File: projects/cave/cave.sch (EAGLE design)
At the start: 111 parts, among them U1 IRLML6344TRPBF, U10 IRLML6344TRPBF, U11 IRLML6344TRPBF, U12 IRLML6344TRPBF, U2 TLC555CDR, U3 IRLML6344TRPBF, U4 IRLML6344TRPBF, U5 IRLML6344TRPBF, U6 IRLML6344TRPBF, U7 TPS54625, U9 IRLML6344TRPBF

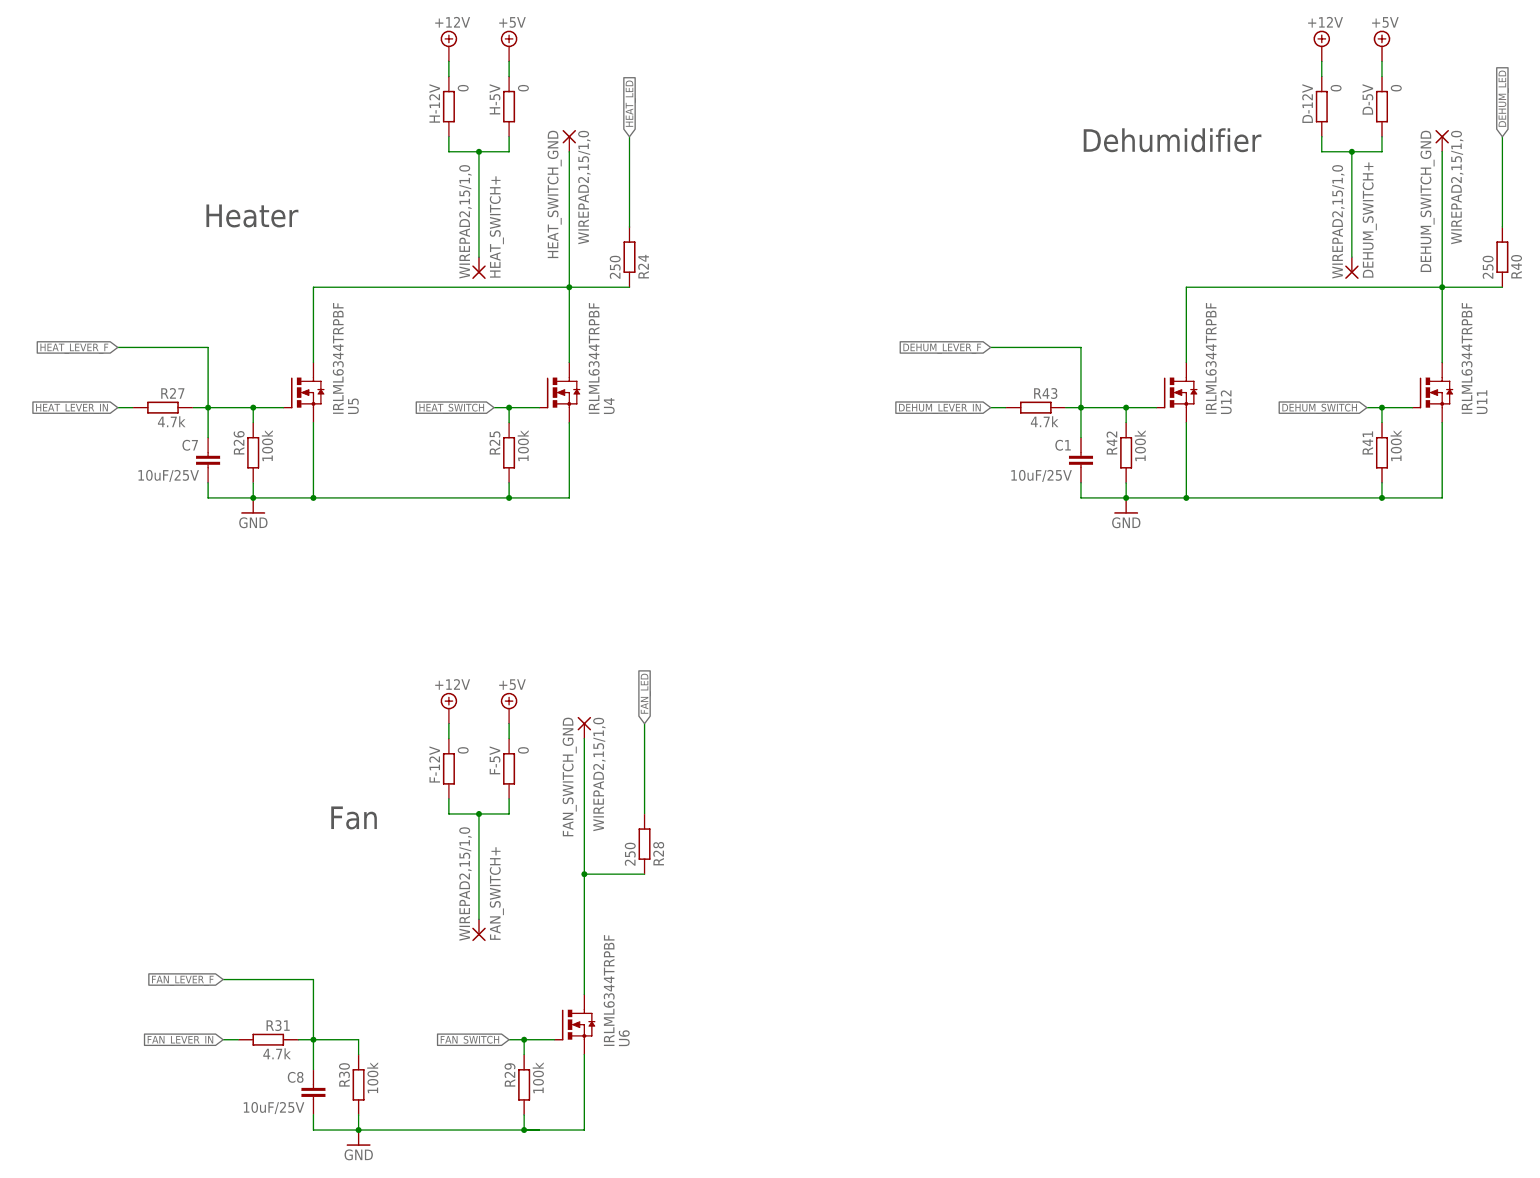
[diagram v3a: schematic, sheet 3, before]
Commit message: Changed 250ohm-0603 led res to 255ohm-0805. Generated BOM
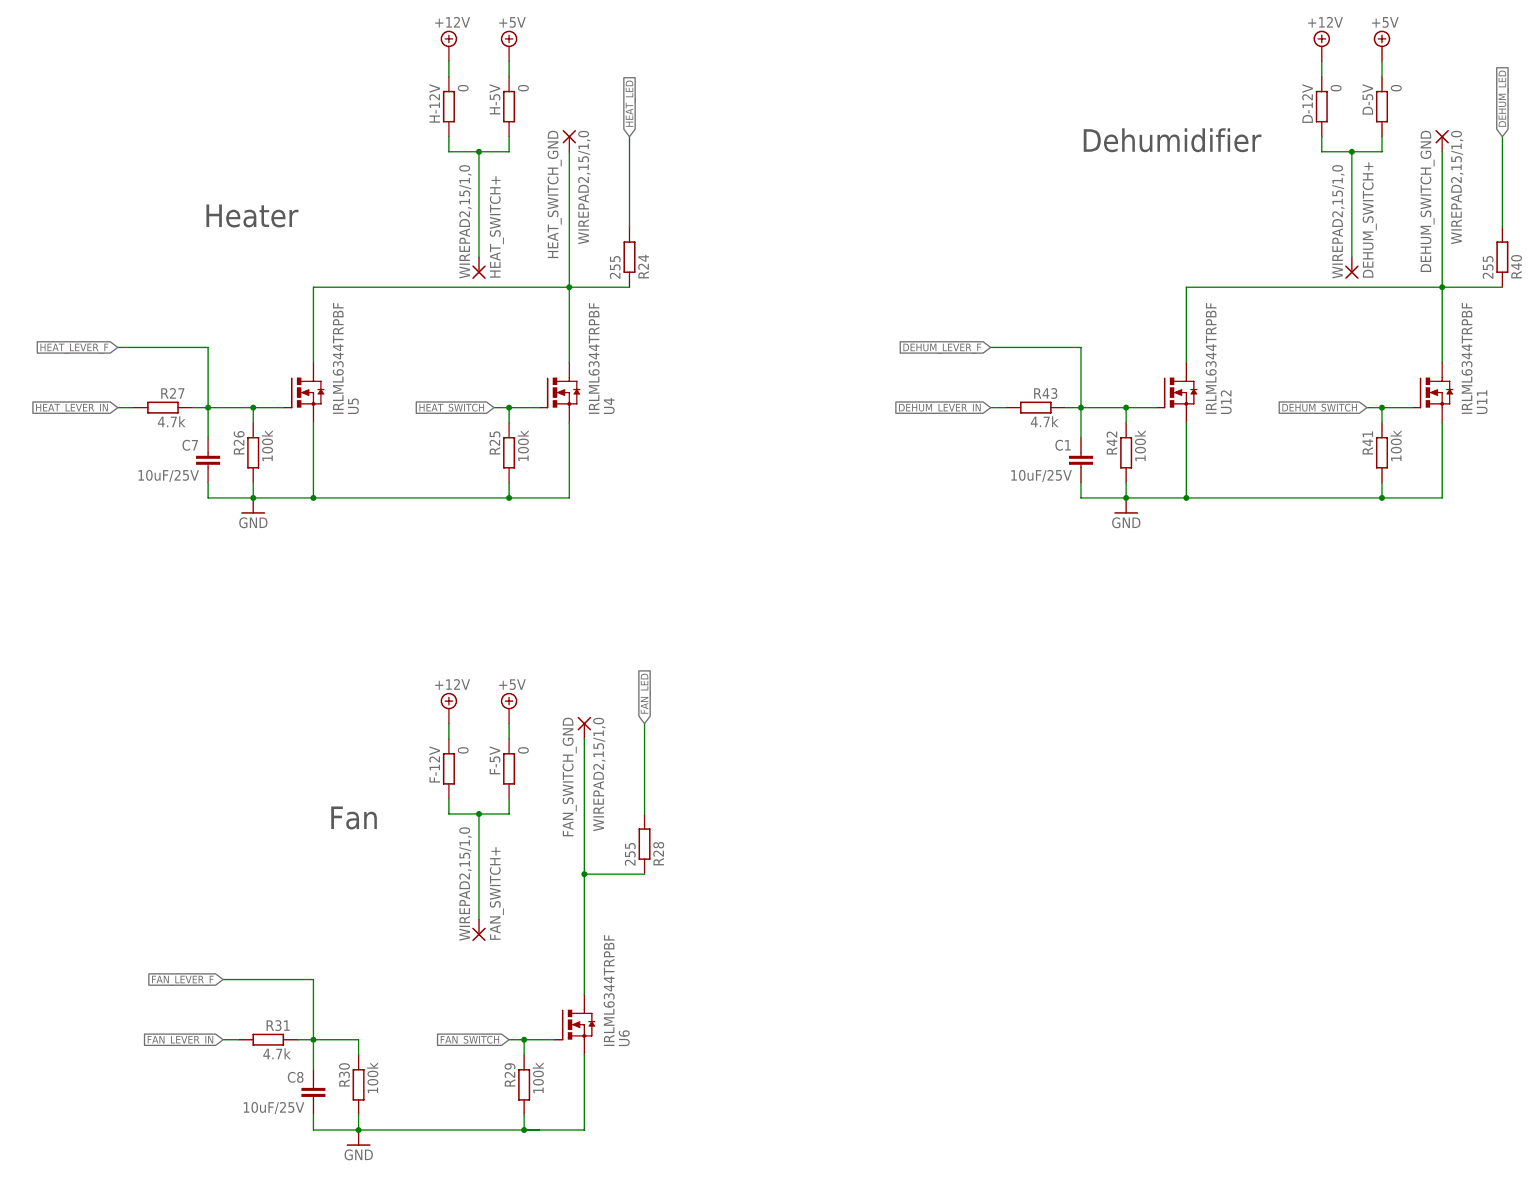
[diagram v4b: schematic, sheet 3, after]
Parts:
- R24, R28, R36, R38, R40: value 250 -> 255; device rcl:R-EU_R0603 -> rcl:R-EU_R0805
- R32: value 100k 1% -> 100k
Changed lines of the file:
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@@
 <grid distance="0.1" unitdist="inch" unit="inch" style="lines" multiple="1" display="no" altdistance="0.01" altunitdist="inch" altunit="inch"/>
 <layers>
-<layer number="1" name="Top" color="4" fill="1" visible="no" active="no"/>
-<layer number="2" name="Route2" color="1" fill="3" visible="no" active="no"/>
-<layer number="3" name="Route3" color="4" fill="3" visible="no" active="no"/>
-<layer number="14" name="Route14" color="1" fill="6" visible="no" active="no"/>
-<layer number="15" name="Route15" color="4" fill="6" visible="no" active="no"/>
-<layer number="16" name="Bottom" color="1" fill="1" visible="no" active="no"/>
-<layer number="17" name="Pads" color="2" fill="1" visible="no" active="no"/>
-<layer number="18" name="Vias" color="2" fill="1" visible="no" active="no"/>
-<layer number="19" name="Unrouted" color="6" fill="1" visible="no" active="no"/>
-<layer number="20" name="Dimension" color="15" fill="1" visible="no" active="no"/>
-<layer number="21" name="tPlace" color="7" fill="1" visible="no" active="no"/>
-<layer number="22" name="bPlace" color="7" fill="1" visible="no" active="no"/>
-<layer number="23" name="tOrigins" color="15" fill="1" visible="no" active="no"/>
-<layer number="24" name="bOrigins" color="15" fill="1" visible="no" active="no"/>
-<layer number="25" name="tNames" color="7" fill="1" visible="no" active="no"/>
-<layer number="26" name="bNames" color="7" fill="1" visible="no" active="no"/>
-<layer number="27" name="tValues" color="7" fill="1" visible="no" active="no"/>
-<layer number="28" name="bValues" color="7" fill="1" visible="no" active="no"/>
+<layer number="1" name="Top" color="4" fill="1" visible="yes" active="no"/>
+<layer number="2" name="Route2" color="1" fill="3" visible="yes" active="no"/>
+<layer number="3" name="Route3" color="4" fill="3" visible="yes" active="no"/>
+<layer number="14" name="Route14" color="1" fill="6" visible="yes" active="no"/>
+<layer number="15" name="Route15" color="4" fill="6" visible="yes" active="no"/>
+<layer number="16" name="Bottom" color="1" fill="1" visible="yes" active="no"/>
+<layer number="17" name="Pads" color="2" fill="1" visible="yes" active="no"/>
+<layer number="18" name="Vias" color="2" fill="1" visible="yes" active="no"/>
+<layer number="19" name="Unrouted" color="6" fill="1" visible="yes" active="no"/>
+<layer number="20" name="Dimension" color="15" fill="1" visible="yes" active="no"/>
+<layer number="21" name="tPlace" color="7" fill="1" visible="yes" active="no"/>
+<layer number="22" name="bPlace" color="7" fill="1" visible="yes" active="no"/>
+<layer number="23" name="tOrigins" color="15" fill="1" visible="yes" active="no"/>
+<layer number="24" name="bOrigins" color="15" fill="1" visible="yes" active="no"/>
+<layer number="25" name="tNames" color="7" fill="1" visible="yes" active="no"/>
+<layer number="26" name="bNames" color="7" fill="1" visible="yes" active="no"/>
+<layer number="27" name="tValues" color="7" fill="1" visible="yes" active="no"/>
+<layer number="28" name="bValues" color="7" fill="1" visible="yes" active="no"/>
 <layer number="29" name="tStop" color="7" fill="3" visible="no" active="no"/>
 <layer number="30" name="bStop" color="7" fill="6" visible="no" active="no"/>
@@
 <layer number="35" name="tGlue" color="7" fill="4" visible="no" active="no"/>
 <layer number="36" name="bGlue" color="7" fill="5" visible="no" active="no"/>
-<layer number="37" name="tTest" color="7" fill="1" visible="no" active="no"/>
-<layer number="38" name="bTest" color="7" fill="1" visible="no" active="no"/>
+<layer number="37" name="tTest" color="7" fill="1" visible="yes" active="no"/>
+<layer number="38" name="bTest" color="7" fill="1" visible="yes" active="no"/>
 <layer number="39" name="tKeepout" color="4" fill="11" visible="no" active="no"/>
 <layer number="40" name="bKeepout" color="1" fill="11" visible="no" active="no"/>
@@
 <layer number="44" name="Drills" color="7" fill="1" visible="no" active="no"/>
 <layer number="45" name="Holes" color="7" fill="1" visible="no" active="no"/>
-<layer number="46" name="Milling" color="3" fill="1" visible="no" active="no"/>
-<layer number="47" name="Measures" color="7" fill="1" visible="no" active="no"/>
-<layer number="48" name="Document" color="7" fill="1" visible="no" active="no"/>
-<layer number="49" name="Reference" color="7" fill="1" visible="no" active="no"/>
-<layer number="50" name="dxf" color="7" fill="1" visible="no" active="no"/>
-<layer number="51" name="tDocu" color="7" fill="1" visible="no" active="no"/>
-<layer number="52" name="bDocu" color="7" fill="1" visible="no" active="no"/>
-<layer number="53" name="tGND_GNDA" color="7" fill="9" visible="no" active="no"/>
-<layer number="54" name="bGND_GNDA" color="1" fill="9" visible="no" active="no"/>
-<layer number="56" name="wert" color="7" fill="1" visible="no" active="no"/>
-<layer number="59" name="Invisible" color="7" fill="1" visible="no" active="no"/>
-<layer number="61" name="stand" color="7" fill="1" visible="no" active="no"/>
+<layer number="46" name="Milling" color="3" fill="1" visible="yes" active="no"/>
+<layer number="47" name="Measures" color="7" fill="1" visible="yes" active="no"/>
+<layer number="48" name="Document" color="7" fill="1" visible="yes" active="no"/>
+<layer number="49" name="Reference" color="7" fill="1" visible="yes" active="no"/>
+<layer number="50" name="dxf" color="7" fill="1" visible="yes" active="no"/>
+<layer number="51" name="tDocu" color="7" fill="1" visible="yes" active="no"/>
+<layer number="52" name="bDocu" color="7" fill="1" visible="yes" active="no"/>
+<layer number="53" name="tGND_GNDA" color="7" fill="9" visible="yes" active="no"/>
+<layer number="54" name="bGND_GNDA" color="1" fill="9" visible="yes" active="no"/>
+<layer number="56" name="wert" color="7" fill="1" visible="yes" active="no"/>
+<layer number="59" name="Invisible" color="7" fill="1" visible="yes" active="no"/>
+<layer number="61" name="stand" color="7" fill="1" visible="yes" active="no"/>
 <layer number="90" name="Modules" color="5" fill="1" visible="yes" active="yes"/>
 <layer number="91" name="Nets" color="2" fill="1" visible="yes" active="yes"/>
@@
 <part name="R23" library="rcl" deviceset="R-EU_" device="R0603" value="10k"/>
 <part name="HEAT_SWITCH_GND" library="wirepad" deviceset="WIREPAD" device="2,15/1,0" value="WIREPAD2,15/1,0"/>
-<part name="R24" library="rcl" deviceset="R-EU_" device="R0603" value="250"/>
+<part name="R24" library="rcl" deviceset="R-EU_" device="R0805" value="255"/>
 <part name="U4" library="transistor-power" deviceset="IRLML6344TRPBF" device=""/>
 <part name="R25" library="rcl" deviceset="R-EU_" device="R0603" value="100k"/>
@@
 <part name="C7" library="rcl" deviceset="C-EU" device="C0805" value="10uF/25V"/>
 <part name="GND16" library="supply1" deviceset="GND" device=""/>
-<part name="R36" library="rcl" deviceset="R-EU_" device="R0603" value="250"/>
+<part name="R36" library="rcl" deviceset="R-EU_" device="R0805" value="255"/>
 <part name="GND17" library="supply1" deviceset="GND" device=""/>
 <part name="U9" library="transistor-power" deviceset="IRLML6344TRPBF" device=""/>
 <part name="R37" library="rcl" deviceset="R-EU_" device="R0603" value="10k"/>
-<part name="R38" library="rcl" deviceset="R-EU_" device="R0603" value="250"/>
+<part name="R38" library="rcl" deviceset="R-EU_" device="R0805" value="255"/>
 <part name="FRAME1" library="frames" deviceset="FRAME_A_L" device=""/>
 <part name="BUZZER+" library="wirepad" deviceset="WIREPAD" device="2,15/1,0" value="WIREPAD2,15/1,0"/>
@@
 <part name="GND21" library="supply1" deviceset="GND" device=""/>
 <part name="DEHUM_SWITCH_GND" library="wirepad" deviceset="WIREPAD" device="2,15/1,0" value="WIREPAD2,15/1,0"/>
-<part name="R40" library="rcl" deviceset="R-EU_" device="R0603" value="250"/>
+<part name="R40" library="rcl" deviceset="R-EU_" device="R0805" value="255"/>
 <part name="U11" library="transistor-power" deviceset="IRLML6344TRPBF" device=""/>
 <part name="R41" library="rcl" deviceset="R-EU_" device="R0603" value="100k"/>
@@
 <part name="FAN_SWITCH_GND" library="wirepad" deviceset="WIREPAD" device="2,15/1,0" value="WIREPAD2,15/1,0"/>
 <part name="FAN_SWITCH+" library="wirepad" deviceset="WIREPAD" device="2,15/1,0" value="WIREPAD2,15/1,0"/>
-<part name="R28" library="rcl" deviceset="R-EU_" device="R0603" value="250"/>
+<part name="R28" library="rcl" deviceset="R-EU_" device="R0805" value="255"/>
 <part name="U6" library="transistor-power" deviceset="IRLML6344TRPBF" device=""/>
 <part name="R29" library="rcl" deviceset="R-EU_" device="R0603" value="100k"/>
@@
 <part name="C11" library="rcl" deviceset="C-EU" device="C0603" value="0.1uF/50V"/>
 <part name="C18" library="rcl" deviceset="C-EU" device="C0603" value="1uF/25V"/>
-<part name="R32" library="rcl" deviceset="R-EU_" device="R0603" value="100k 1%"/>
+<part name="R32" library="rcl" deviceset="R-EU_" device="R0603" value="100k"/>
 <part name="C19" library="rcl" deviceset="C-EU" device="C0603" value="8200pF/50V"/>
 <part name="R34" library="rcl" deviceset="R-EU_" device="R0603" value="124k 1%"/>
